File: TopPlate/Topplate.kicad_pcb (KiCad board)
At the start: 2 copper layers, 158.1 x 94.8 mm, 0 parts

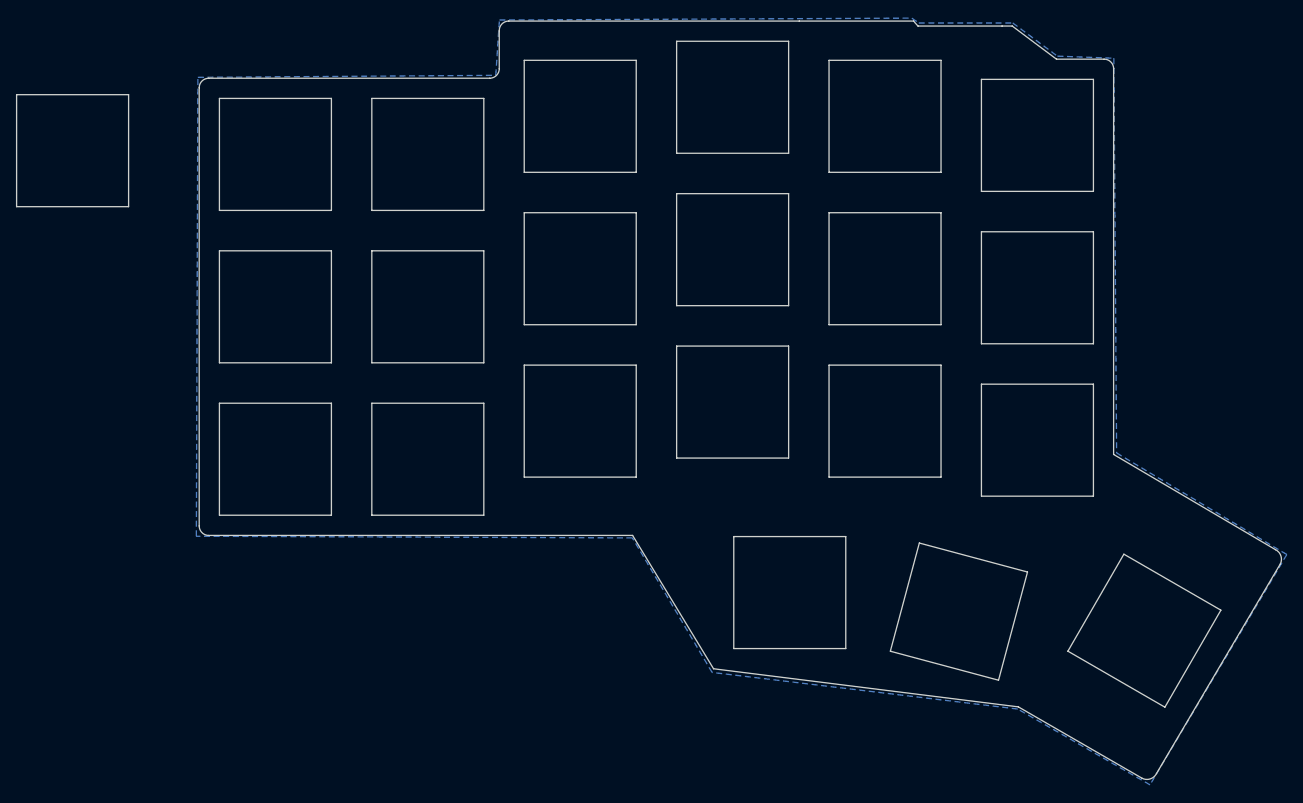
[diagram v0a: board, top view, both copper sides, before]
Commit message: Add back and front layer
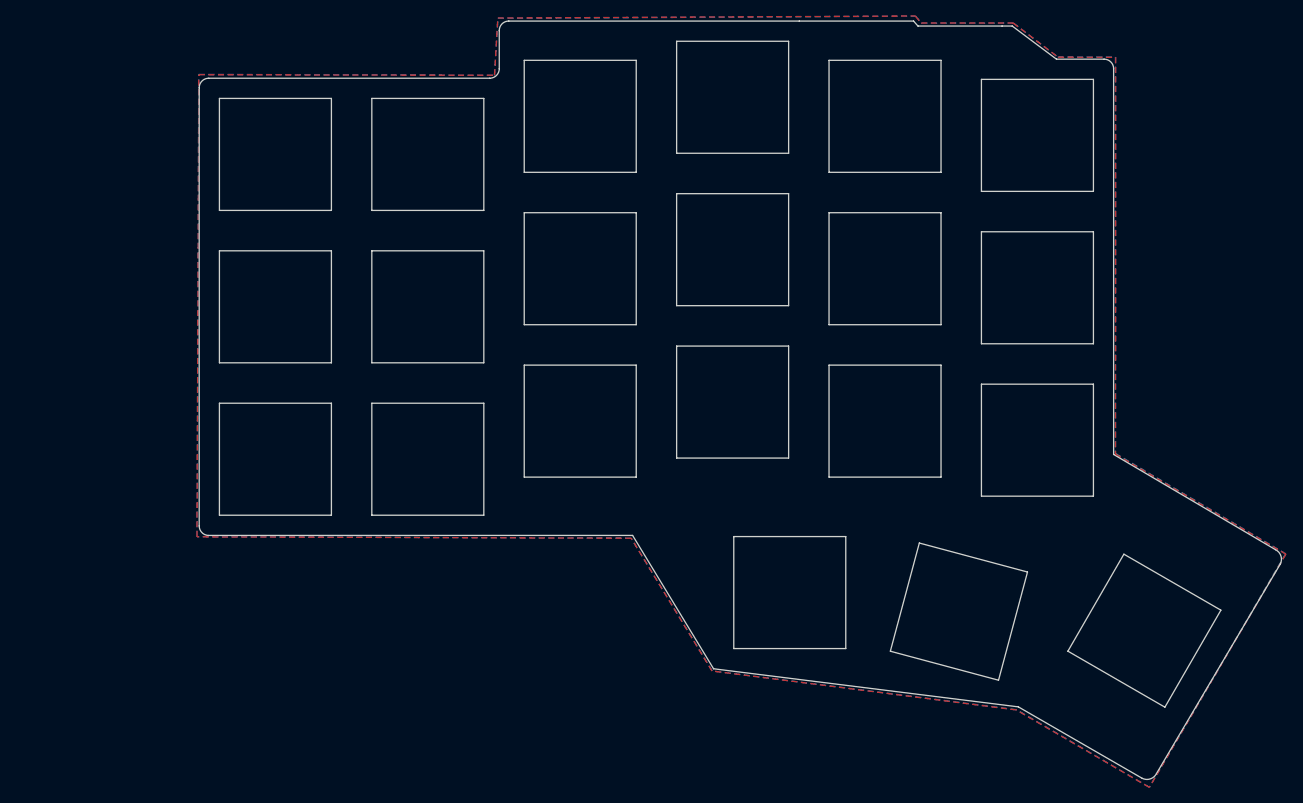
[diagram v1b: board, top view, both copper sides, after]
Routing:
- added copper zone on F.Cu, net (none)
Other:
- board size 158.1 x 94.8 mm -> 135.3 x 94.8 mm

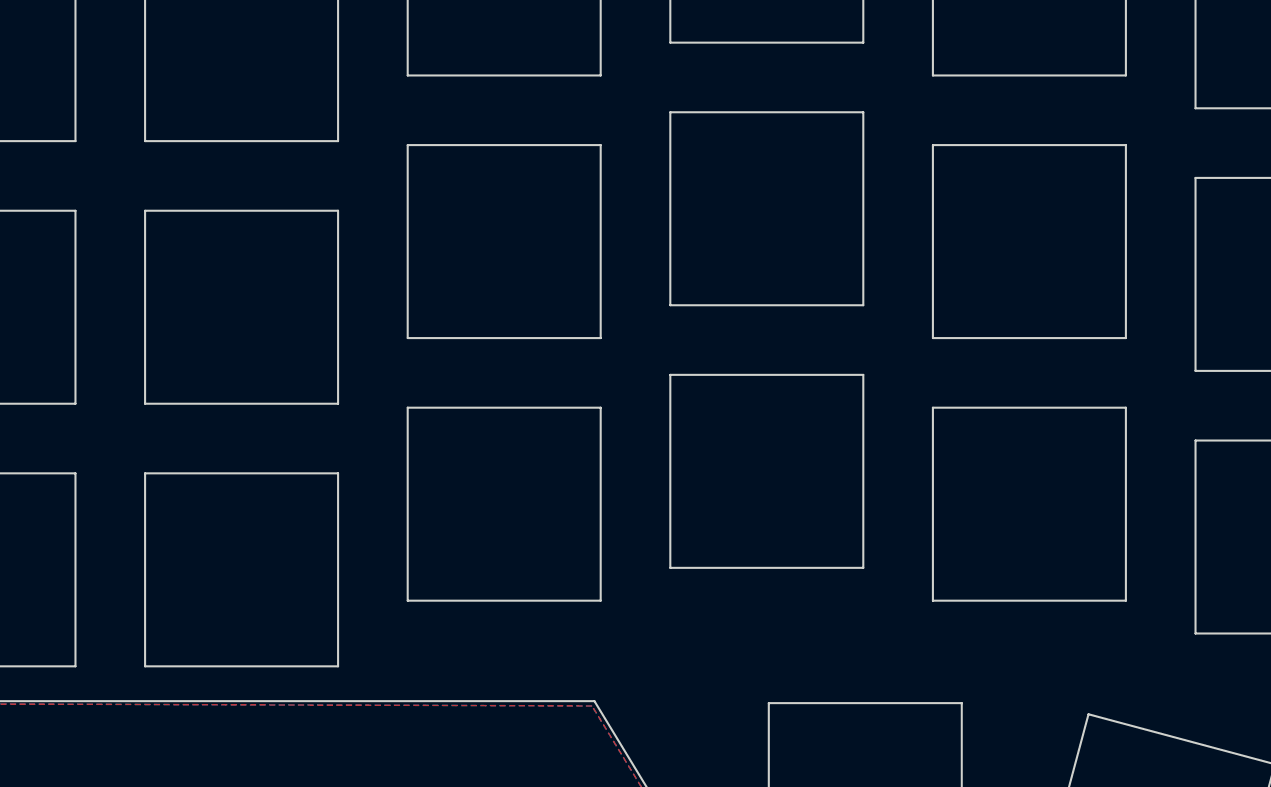
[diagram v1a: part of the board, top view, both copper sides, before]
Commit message: Add holes for screws
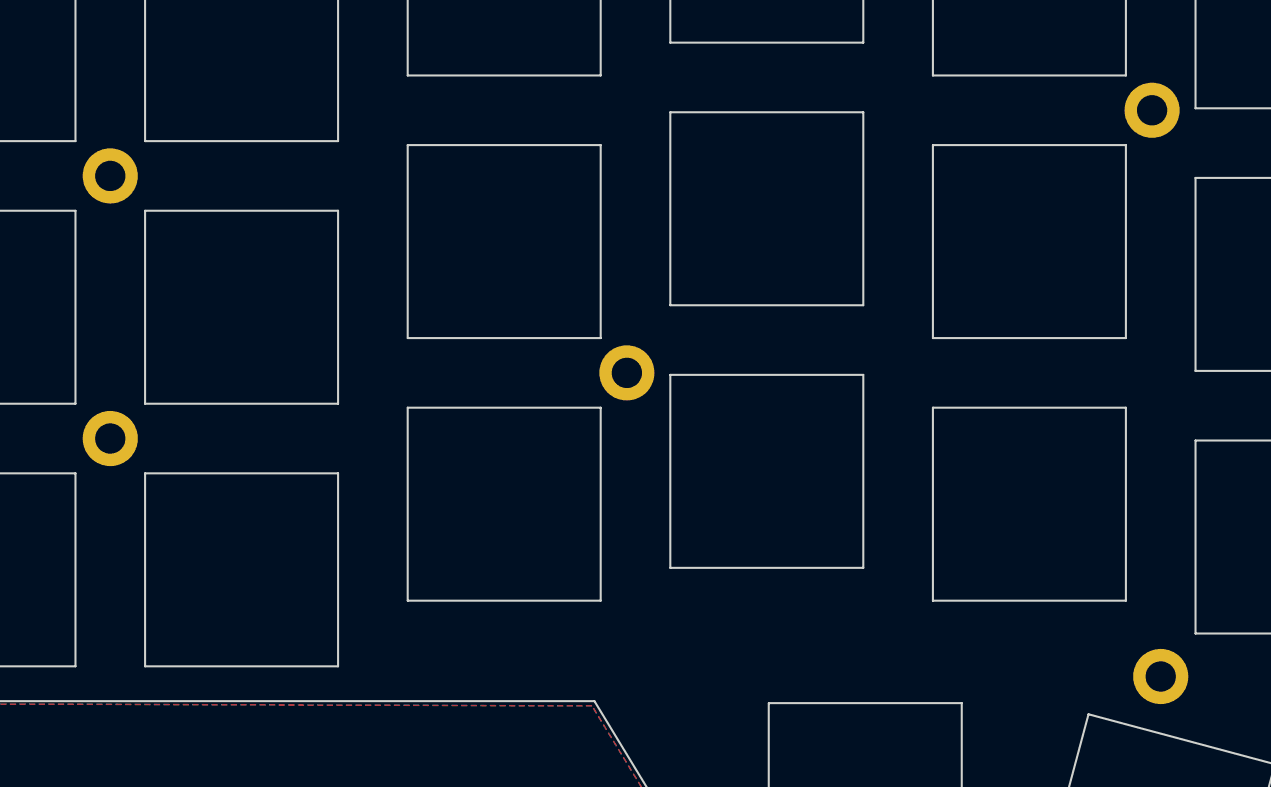
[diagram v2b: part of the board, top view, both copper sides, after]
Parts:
- added ?: , kbd:LEGO_HOLE, F.Cu at (185.2, 122.5)
- added ?: , kbd:LEGO_HOLE, F.Cu at (184.6, 81.4)
- added ?: , kbd:LEGO_HOLE, F.Cu at (146.5, 100.4)
- added ?: , kbd:LEGO_HOLE, F.Cu at (109.0, 105.2)
- added ?: , kbd:LEGO_HOLE, F.Cu at (109.0, 86.2)
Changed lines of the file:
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@@
     (tracks 0)
     (zones 0)
-    (modules 0)
+    (modules 5)
     (nets 1)
   )
@@
     (uvia_drill 0.1)
   )
+  (module kbd:LEGO_HOLE (layer F.Cu)
+    (at 185.20878 122.46928)
+    (descr "Mounting Hole 2.2mm, no annular, M2")
+    (tags "mounting hole 2.2mm no annular m2")
+    (attr virtual)
+    (fp_text reference "" (at 0 -3.2) (layer F.SilkS)
+      (effects (font (size 1 1) (thickness 0.15)))
+    )
+    (fp_text value "" (at 0 3.2) (layer F.Fab)
+      (effects (font (size 1 1) (thickness 0.15)))
+    )
+    (fp_circle (center 0 0) (end 2.45 0) (layer F.CrtYd) (width 0.05))
+    (fp_circle (center 0 0) (end 2.2 0) (layer Cmts.User) (width 0.15))
+    (fp_text user %R (at 0.3 0) (layer F.Fab)
+      (effects (font (size 1 1) (thickness 0.15)))
+    )
+    (pad "" thru_hole circle (at 0 0) (size 4 4) (drill 2.2) (layers *.Cu *.Mask))
+  )
+  (module kbd:LEGO_HOLE (layer F.Cu)
+    (at 184.58278 81.39428)
+    (descr "Mounting Hole 2.2mm, no annular, M2")
+    (tags "mounting hole 2.2mm no annular m2")
+    (attr virtual)
+    (fp_text reference "" (at 0 -3.2) (layer F.SilkS)
+      (effects (font (size 1 1) (thickness 0.15)))
+    )
+    (fp_text value "" (at 0 3.2) (layer F.Fab)
+      (effects (font (size 1 1) (thickness 0.15)))
+    )
+    (fp_circle (center 0 0) (end 2.45 0) (layer F.CrtYd) (width 0.05))
+    (fp_circle (center 0 0) (end 2.2 0) (layer Cmts.User) (width 0.15))
+    (fp_text user %R (at 0.3 0) (layer F.Fab)
+      (effects (font (size 1 1) (thickness 0.15)))
+    )
+    (pad "" thru_hole circle (at 0 0) (size 4 4) (drill 2.2) (layers *.Cu *.Mask))
+  )
+  (module kbd:LEGO_HOLE (layer F.Cu)
+    (at 146.48278 100.44428)
+    (descr "Mounting Hole 2.2mm, no annular, M2")
+    (tags "mounting hole 2.2mm no annular m2")
+    (attr virtual)
+    (fp_text reference "" (at 0 -3.2) (layer F.SilkS)
+      (effects (font (size 1 1) (thickness 0.15)))
+    )
+    (fp_text value "" (at 0 3.2) (layer F.Fab)
+      (effects (font (size 1 1) (thickness 0.15)))
+    )
+    (fp_text user %R (at 0.3 0) (layer F.Fab)
+      (effects (font (size 1 1) (thickness 0.15)))
+    )
+    (fp_circle (center 0 0) (end 2.2 0) (layer Cmts.User) (width 0.15))
+    (fp_circle (center 0 0) (end 2.45 0) (layer F.CrtYd) (width 0.05))
+    (pad "" thru_hole circle (at 0 0) (size 4 4) (drill 2.2) (layers *.Cu *.Mask))
+  )
+  (module kbd:LEGO_HOLE (layer F.Cu)
+    (at 109.00753 105.20678)
+    (descr "Mounting Hole 2.2mm, no annular, M2")
+    (tags "mounting hole 2.2mm no annular m2")
+    (attr virtual)
+    (fp_text reference "" (at 0 -3.2) (layer F.SilkS)
+      (effects (font (size 1 1) (thickness 0.15)))
+    )
+    (fp_text value "" (at 0 3.2) (layer F.Fab)
+      (effects (font (size 1 1) (thickness 0.15)))
+    )
+    (fp_circle (center 0 0) (end 2.45 0) (layer F.CrtYd) (width 0.05))
+    (fp_circle (center 0 0) (end 2.2 0) (layer Cmts.User) (width 0.15))
+    (fp_text user %R (at 0.3 0) (layer F.Fab)
+      (effects (font (size 1 1) (thickness 0.15)))
+    )
+    (pad "" thru_hole circle (at 0 0) (size 4 4) (drill 2.2) (layers *.Cu *.Mask))
+  )
+  (module kbd:LEGO_HOLE (layer F.Cu)
+    (at 109.00753 86.15678)
+    (descr "Mounting Hole 2.2mm, no annular, M2")
+    (tags "mounting hole 2.2mm no annular m2")
+    (attr virtual)
+    (fp_text reference "" (at 0 -3.2) (layer F.SilkS)
+      (effects (font (size 1 1) (thickness 0.15)))
+    )
+    (fp_text value "" (at 0 3.2) (layer F.Fab)
+      (effects (font (size 1 1) (thickness 0.15)))
+    )
+    (fp_circle (center 0 0) (end 2.45 0) (layer F.CrtYd) (width 0.05))
+    (fp_circle (center 0 0) (end 2.2 0) (layer Cmts.User) (width 0.15))
+    (fp_text user %R (at 0.3 0) (layer F.Fab)
+      (effects (font (size 1 1) (thickness 0.15)))
+    )
+    (pad "" thru_hole circle (at 0 0) (size 4 4) (drill 2.2) (layers *.Cu *.Mask))
+  )
   (gr_line (start 210.665958 145.725208) (end 198.541602 138.725208) (layer Edge.Cuts) (width 0.15))

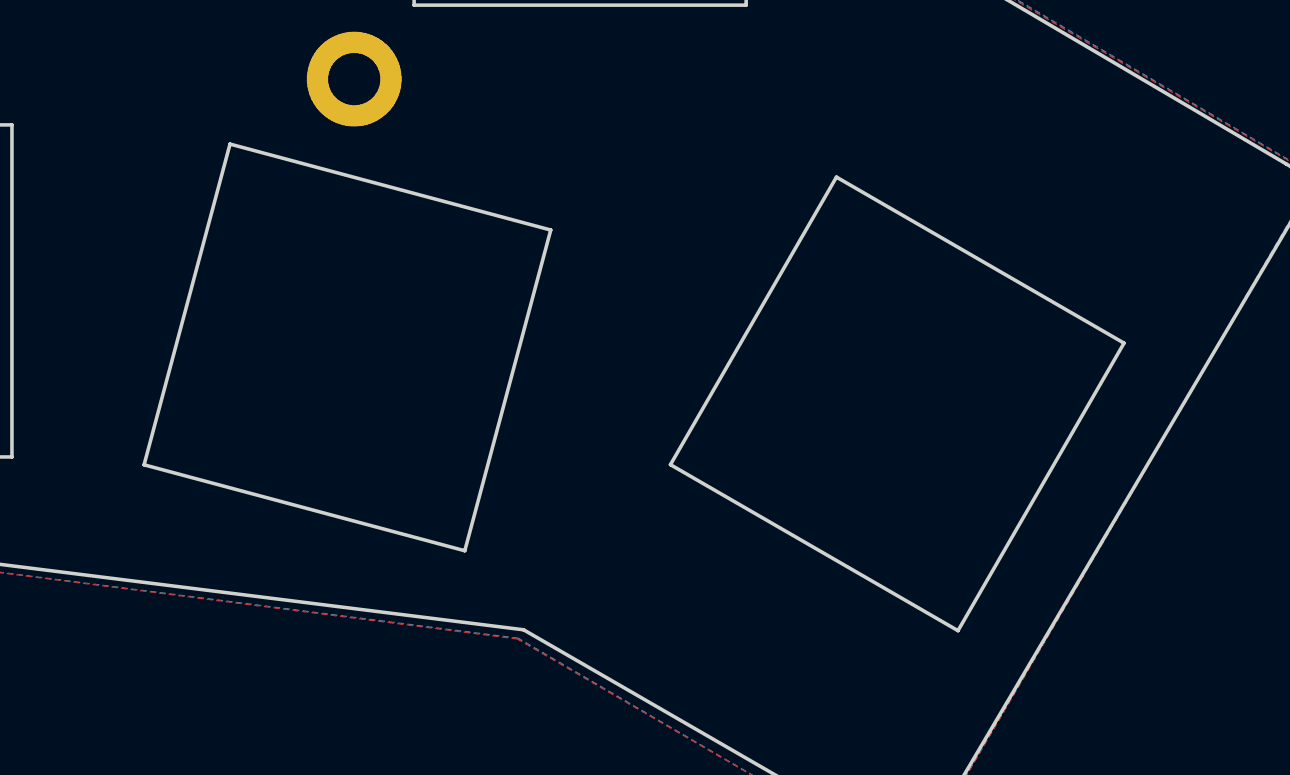
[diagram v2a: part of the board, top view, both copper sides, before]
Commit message: Adjust position errors on rotated keys
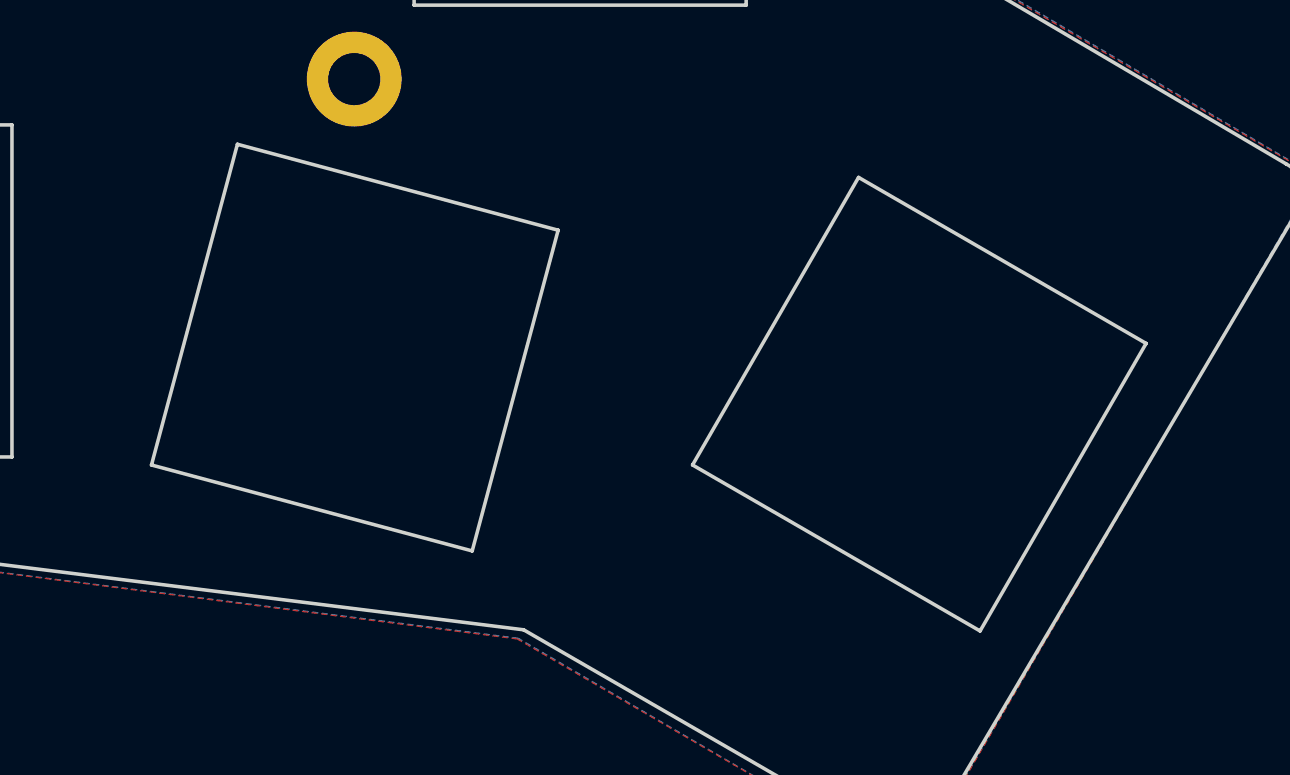
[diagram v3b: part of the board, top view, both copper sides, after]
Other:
- outline, holes or cut-outs redrawn
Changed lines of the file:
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@@
     (pad "" thru_hole circle (at 0 0) (size 4 4) (drill 2.2) (layers *.Cu *.Mask))
   )
-  (gr_line (start 210.665958 145.725208) (end 198.541602 138.725208) (layer Edge.Cuts) (width 0.15))
-  (gr_line (start 198.541602 138.725208) (end 205.541602 126.600852) (layer Edge.Cuts) (width 0.15))
-  (gr_line (start 205.541602 126.600852) (end 217.665958 133.600852) (layer Edge.Cuts) (width 0.15))
-  (gr_line (start 210.665958 145.725208) (end 217.665958 133.600852) (layer Edge.Cuts) (width 0.15))
-  (gr_line (start 176.348066 138.731527) (end 179.971533 125.208566) (layer Edge.Cuts) (width 0.15))
-  (gr_line (start 179.971533 125.208566) (end 193.494494 128.832033) (layer Edge.Cuts) (width 0.15))
-  (gr_line (start 193.494494 128.832033) (end 189.871027 142.354994) (layer Edge.Cuts) (width 0.15))
-  (gr_line (start 176.348066 138.731527) (end 189.871027 142.354994) (layer Edge.Cuts) (width 0.15))
+  (gr_line (start 211.597448 145.737908) (end 199.473092 138.737908) (layer Edge.Cuts) (width 0.15))
+  (gr_line (start 199.473092 138.737908) (end 206.473092 126.613552) (layer Edge.Cuts) (width 0.15))
+  (gr_line (start 206.473092 126.613552) (end 218.597448 133.613552) (layer Edge.Cuts) (width 0.15))
+  (gr_line (start 211.597448 145.737908) (end 218.597448 133.613552) (layer Edge.Cuts) (width 0.15))
+  (gr_line (start 176.659715 138.739146) (end 180.283183 125.216184) (layer Edge.Cuts) (width 0.15))
+  (gr_line (start 180.283183 125.216184) (end 193.806145 128.839652) (layer Edge.Cuts) (width 0.15))
+  (gr_line (start 193.806145 128.839652) (end 190.182677 142.362614) (layer Edge.Cuts) (width 0.15))
+  (gr_line (start 176.659715 138.739146) (end 190.182677 142.362614) (layer Edge.Cuts) (width 0.15))
   (gr_line (start 156.77753 138.40053) (end 156.77753 124.40053) (layer Edge.Cuts) (width 0.15))
   (gr_line (start 156.77753 124.40053) (end 170.77753 124.40053) (layer Edge.Cuts) (width 0.15))
@@
     (polygon
       (pts
-        (xy 180.121533 125.358566) (xy 176.575712 138.59175) (xy 189.808896 142.137571) (xy 193.354717 128.904387)
-      )
-    )
-  )
-  (zone (net 0) (net_name "") (layers F&B.Cu) (hatch edge 0.508)
-    (connect_pads (clearance 0.508))
-    (min_thickness 0.254)
-    (keepout (tracks not_allowed) (vias not_allowed) (copperpour not_allowed))
-    (fill (arc_segments 16) (thermal_gap 0.508) (thermal_bridge_width 0.508))
-    (polygon
-      (pts
-        (xy 198.754699 138.672967) (xy 210.619247 145.522967) (xy 217.469247 133.658419) (xy 205.604699 126.808419)
-      )
-    )
+        (xy 180.433183 125.366184) (xy 176.887362 138.599368) (xy 190.120546 142.145189) (xy 193.666367 128.912005)
+      )
+    )
+  )
+  (zone (net 0) (net_name "") (layers F&B.Cu) (hatch edge 0.508)
+    (connect_pads (clearance 0.508))
+    (min_thickness 0.254)
+    (keepout (tracks not_allowed) (vias not_allowed) (copperpour not_allowed))
+    (fill (arc_segments 16) (thermal_gap 0.508) (thermal_bridge_width 0.508))
+    (polygon
+      (pts
+        (xy 199.692563 138.661493) (xy 211.557111 145.511493) (xy 218.407111 133.646945) (xy 206.542563 126.796945)
+      )
+    )
